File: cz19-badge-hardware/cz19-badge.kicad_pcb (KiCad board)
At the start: 4 copper layers, 169 x 56 mm, 210 parts, among them J1 USB_B_Micro, Q1 MMBT2222A, Q2 MMBT2222A, Q3 FDS8896, U1 CH340C, U2 ESP32-WROOM-32D, U3 AMS1117

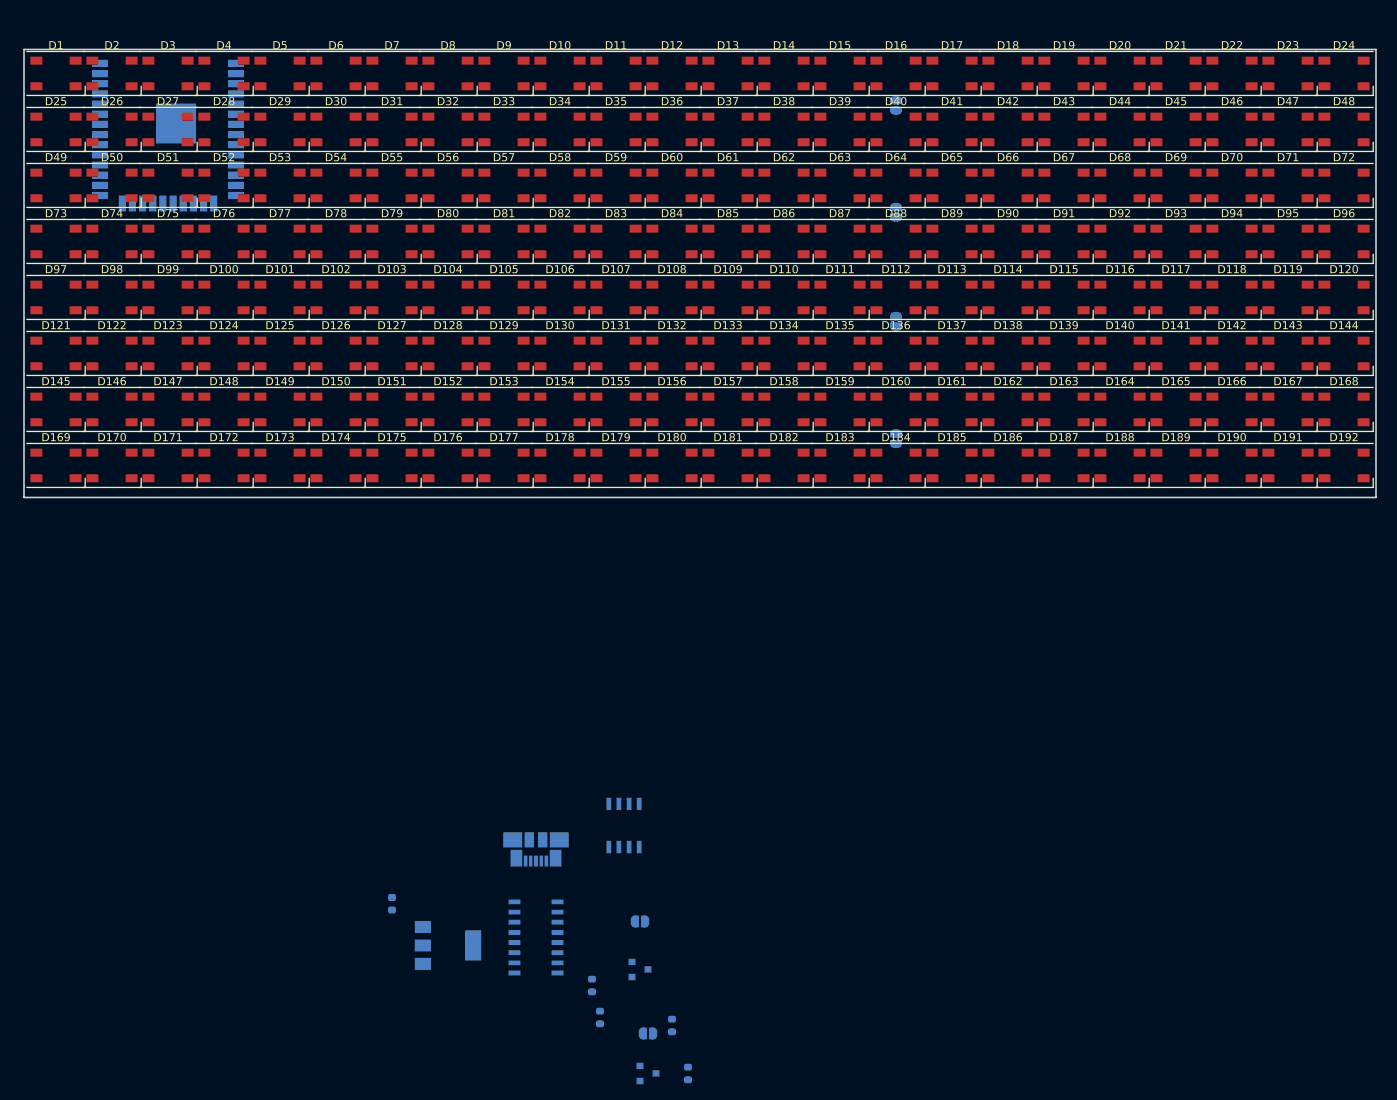
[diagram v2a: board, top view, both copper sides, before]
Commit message: Added battery, organised components, layed out PCB. Working on PCB traces of LED matrix
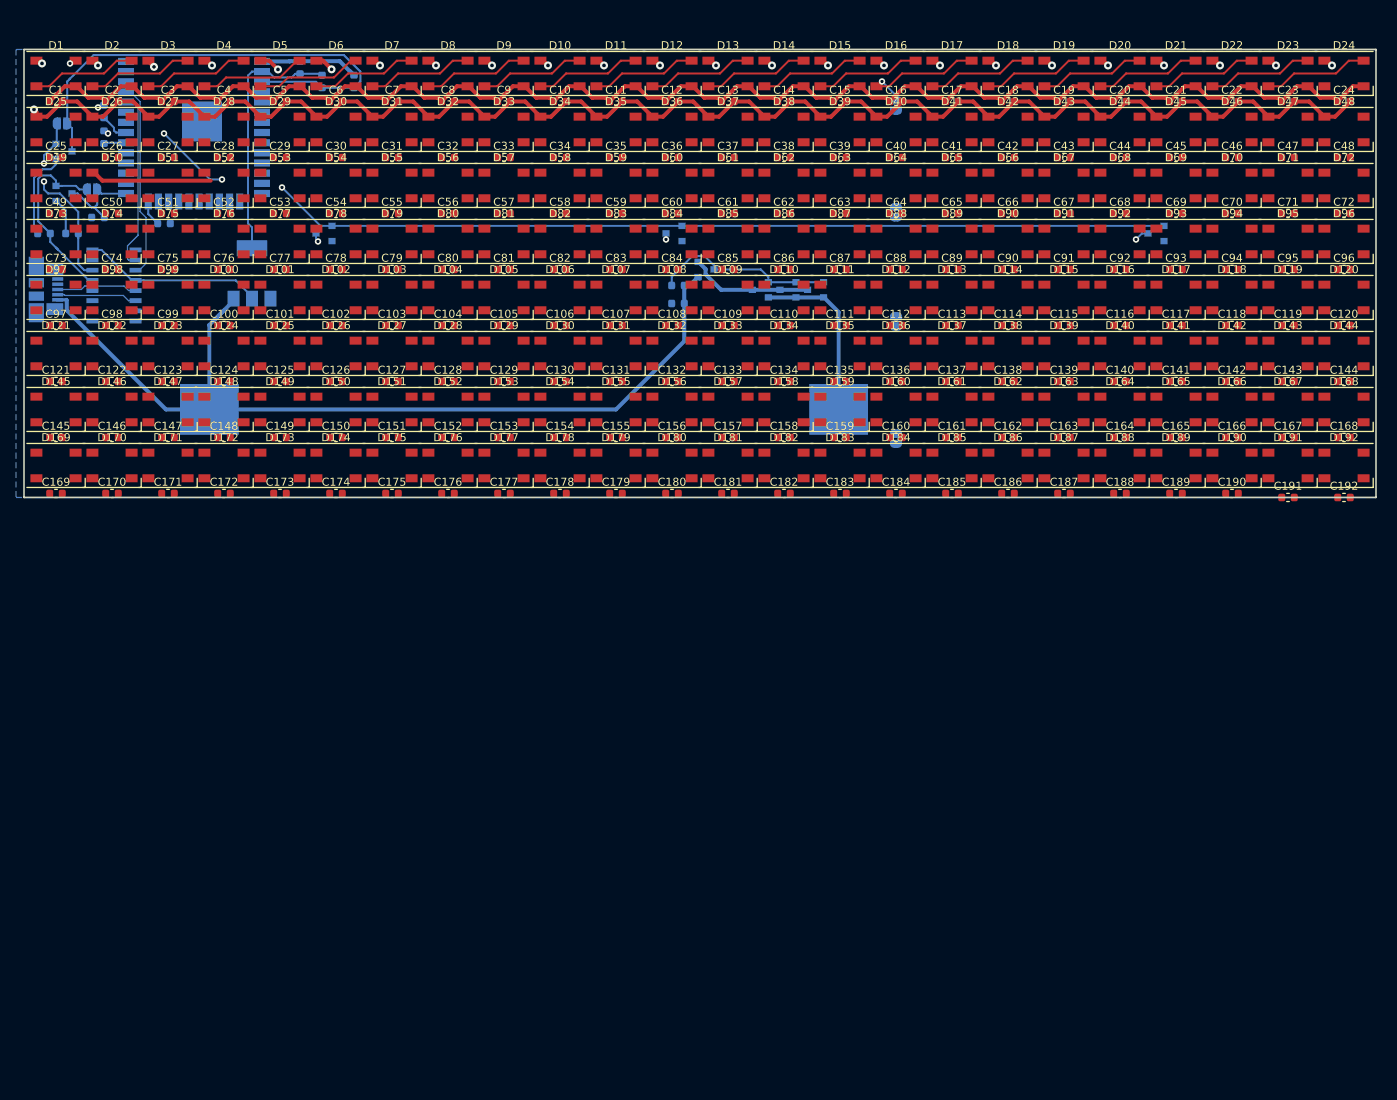
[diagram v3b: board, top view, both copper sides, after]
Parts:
- removed R2: 10k, Resistor_SMD:R_0603_1608Metric
- added BT1: Battery, LiPoHolder:BatteryHolder_Keystone_1042_1x18650, B.Cu at (82.5, 67.0)
- added C1: 100nF, Capacitor_SMD:C_0603_1608Metric, F.Cu at (24.0, 28.5)
- added C10: 100nF, Capacitor_SMD:C_0603_1608Metric, F.Cu at (87.0, 28.5)
- added C100: 100nF, Capacitor_SMD:C_0603_1608Metric, F.Cu at (45.0, 56.5)
- added C101: 100nF, Capacitor_SMD:C_0603_1608Metric, F.Cu at (52.0, 56.5)
- added C102: 100nF, Capacitor_SMD:C_0603_1608Metric, F.Cu at (59.0, 56.5)
- added C103: 100nF, Capacitor_SMD:C_0603_1608Metric, F.Cu at (66.0, 56.5)
- added C104: 100nF, Capacitor_SMD:C_0603_1608Metric, F.Cu at (73.0, 56.5)
- added C105: 100nF, Capacitor_SMD:C_0603_1608Metric, F.Cu at (80.0, 56.5)
- added C106: 100nF, Capacitor_SMD:C_0603_1608Metric, F.Cu at (87.0, 56.5)
- added C107: 100nF, Capacitor_SMD:C_0603_1608Metric, F.Cu at (94.0, 56.5)
- added C108: 100nF, Capacitor_SMD:C_0603_1608Metric, F.Cu at (101.0, 56.5)
- added C109: 100nF, Capacitor_SMD:C_0603_1608Metric, F.Cu at (108.0, 56.5)
- added C11: 100nF, Capacitor_SMD:C_0603_1608Metric, F.Cu at (94.0, 28.5)
- added C110: 100nF, Capacitor_SMD:C_0603_1608Metric, F.Cu at (115.0, 56.5)
- added C111: 100nF, Capacitor_SMD:C_0603_1608Metric, F.Cu at (122.0, 56.5)
- added C112: 100nF, Capacitor_SMD:C_0603_1608Metric, F.Cu at (129.0, 56.5)
- added C113: 100nF, Capacitor_SMD:C_0603_1608Metric, F.Cu at (136.0, 56.5)
- added C114: 100nF, Capacitor_SMD:C_0603_1608Metric, F.Cu at (143.0, 56.5)
- added C115: 100nF, Capacitor_SMD:C_0603_1608Metric, F.Cu at (150.0, 56.5)
- added C116: 100nF, Capacitor_SMD:C_0603_1608Metric, F.Cu at (157.0, 56.5)
- added C117: 100nF, Capacitor_SMD:C_0603_1608Metric, F.Cu at (164.0, 56.5)
- added C118: 100nF, Capacitor_SMD:C_0603_1608Metric, F.Cu at (171.0, 56.5)
- added C119: 100nF, Capacitor_SMD:C_0603_1608Metric, F.Cu at (178.0, 56.5)
- added C12: 100nF, Capacitor_SMD:C_0603_1608Metric, F.Cu at (101.0, 28.5)
- added C120: 100nF, Capacitor_SMD:C_0603_1608Metric, F.Cu at (185.0, 56.5)
- added C121: 100nF, Capacitor_SMD:C_0603_1608Metric, F.Cu at (24.0, 63.5)
- added C122: 100nF, Capacitor_SMD:C_0603_1608Metric, F.Cu at (31.0, 63.5)
- added C123: 100nF, Capacitor_SMD:C_0603_1608Metric, F.Cu at (38.0, 63.5)
- added C124: 100nF, Capacitor_SMD:C_0603_1608Metric, F.Cu at (45.0, 63.5)
- added C125: 100nF, Capacitor_SMD:C_0603_1608Metric, F.Cu at (52.0, 63.5)
- added C126: 100nF, Capacitor_SMD:C_0603_1608Metric, F.Cu at (59.0, 63.5)
- added C127: 100nF, Capacitor_SMD:C_0603_1608Metric, F.Cu at (66.0, 63.5)
- added C128: 100nF, Capacitor_SMD:C_0603_1608Metric, F.Cu at (73.0, 63.5)
- added C129: 100nF, Capacitor_SMD:C_0603_1608Metric, F.Cu at (80.0, 63.5)
- added C13: 100nF, Capacitor_SMD:C_0603_1608Metric, F.Cu at (108.0, 28.5)
- added C130: 100nF, Capacitor_SMD:C_0603_1608Metric, F.Cu at (87.0, 63.5)
- added C131: 100nF, Capacitor_SMD:C_0603_1608Metric, F.Cu at (94.0, 63.5)
- added C132: 100nF, Capacitor_SMD:C_0603_1608Metric, F.Cu at (101.0, 63.5)
- added C133: 100nF, Capacitor_SMD:C_0603_1608Metric, F.Cu at (108.0, 63.5)
- added C134: 100nF, Capacitor_SMD:C_0603_1608Metric, F.Cu at (115.0, 63.5)
- added C135: 100nF, Capacitor_SMD:C_0603_1608Metric, F.Cu at (122.0, 63.5)
- added C136: 100nF, Capacitor_SMD:C_0603_1608Metric, F.Cu at (129.0, 63.5)
- added C137: 100nF, Capacitor_SMD:C_0603_1608Metric, F.Cu at (136.0, 63.5)
- added C138: 100nF, Capacitor_SMD:C_0603_1608Metric, F.Cu at (143.0, 63.5)
- added C139: 100nF, Capacitor_SMD:C_0603_1608Metric, F.Cu at (150.0, 63.5)
- added C14: 100nF, Capacitor_SMD:C_0603_1608Metric, F.Cu at (115.0, 28.5)
- added C140: 100nF, Capacitor_SMD:C_0603_1608Metric, F.Cu at (157.0, 63.5)
- added C141: 100nF, Capacitor_SMD:C_0603_1608Metric, F.Cu at (164.0, 63.5)
- added C142: 100nF, Capacitor_SMD:C_0603_1608Metric, F.Cu at (171.0, 63.5)
- added C143: 100nF, Capacitor_SMD:C_0603_1608Metric, F.Cu at (178.0, 63.5)
- added C144: 100nF, Capacitor_SMD:C_0603_1608Metric, F.Cu at (185.0, 63.5)
- added C145: 100nF, Capacitor_SMD:C_0603_1608Metric, F.Cu at (24.0, 70.5)
- added C146: 100nF, Capacitor_SMD:C_0603_1608Metric, F.Cu at (31.0, 70.5)
- added C147: 100nF, Capacitor_SMD:C_0603_1608Metric, F.Cu at (38.0, 70.5)
- added C148: 100nF, Capacitor_SMD:C_0603_1608Metric, F.Cu at (45.0, 70.5)
- added C149: 100nF, Capacitor_SMD:C_0603_1608Metric, F.Cu at (52.0, 70.5)
- added C15: 100nF, Capacitor_SMD:C_0603_1608Metric, F.Cu at (122.0, 28.5)
- added C150: 100nF, Capacitor_SMD:C_0603_1608Metric, F.Cu at (59.0, 70.5)
- added C151: 100nF, Capacitor_SMD:C_0603_1608Metric, F.Cu at (66.0, 70.5)
- added C152: 100nF, Capacitor_SMD:C_0603_1608Metric, F.Cu at (73.0, 70.5)
- added C153: 100nF, Capacitor_SMD:C_0603_1608Metric, F.Cu at (80.0, 70.5)
- added C154: 100nF, Capacitor_SMD:C_0603_1608Metric, F.Cu at (87.0, 70.5)
- added C155: 100nF, Capacitor_SMD:C_0603_1608Metric, F.Cu at (94.0, 70.5)
- added C156: 100nF, Capacitor_SMD:C_0603_1608Metric, F.Cu at (101.0, 70.5)
- added C157: 100nF, Capacitor_SMD:C_0603_1608Metric, F.Cu at (108.0, 70.5)
- added C158: 100nF, Capacitor_SMD:C_0603_1608Metric, F.Cu at (115.0, 70.5)
- added C159: 100nF, Capacitor_SMD:C_0603_1608Metric, F.Cu at (122.0, 70.5)
- added C16: 100nF, Capacitor_SMD:C_0603_1608Metric, F.Cu at (129.0, 28.5)
- added C160: 100nF, Capacitor_SMD:C_0603_1608Metric, F.Cu at (129.0, 70.5)
- added C161: 100nF, Capacitor_SMD:C_0603_1608Metric, F.Cu at (136.0, 70.5)
- added C162: 100nF, Capacitor_SMD:C_0603_1608Metric, F.Cu at (143.0, 70.5)
- added C163: 100nF, Capacitor_SMD:C_0603_1608Metric, F.Cu at (150.0, 70.5)
- added C164: 100nF, Capacitor_SMD:C_0603_1608Metric, F.Cu at (157.0, 70.5)
- added C165: 100nF, Capacitor_SMD:C_0603_1608Metric, F.Cu at (164.0, 70.5)
- added C166: 100nF, Capacitor_SMD:C_0603_1608Metric, F.Cu at (171.0, 70.5)
- added C167: 100nF, Capacitor_SMD:C_0603_1608Metric, F.Cu at (178.0, 70.5)
- added C168: 100nF, Capacitor_SMD:C_0603_1608Metric, F.Cu at (185.0, 70.5)
- added C169: 100nF, Capacitor_SMD:C_0603_1608Metric, F.Cu at (24.0, 77.5)
- added C17: 100nF, Capacitor_SMD:C_0603_1608Metric, F.Cu at (136.0, 28.5)
- added C170: 100nF, Capacitor_SMD:C_0603_1608Metric, F.Cu at (31.0, 77.5)
- added C171: 100nF, Capacitor_SMD:C_0603_1608Metric, F.Cu at (38.0, 77.5)
- added C172: 100nF, Capacitor_SMD:C_0603_1608Metric, F.Cu at (45.0, 77.5)
- added C173: 100nF, Capacitor_SMD:C_0603_1608Metric, F.Cu at (52.0, 77.5)
- added C174: 100nF, Capacitor_SMD:C_0603_1608Metric, F.Cu at (59.0, 77.5)
- added C175: 100nF, Capacitor_SMD:C_0603_1608Metric, F.Cu at (66.0, 77.5)
- added C176: 100nF, Capacitor_SMD:C_0603_1608Metric, F.Cu at (73.0, 77.5)
- added C177: 100nF, Capacitor_SMD:C_0603_1608Metric, F.Cu at (80.0, 77.5)
- added C178: 100nF, Capacitor_SMD:C_0603_1608Metric, F.Cu at (87.0, 77.5)
- added C179: 100nF, Capacitor_SMD:C_0603_1608Metric, F.Cu at (94.0, 77.5)
- added C18: 100nF, Capacitor_SMD:C_0603_1608Metric, F.Cu at (143.0, 28.5)
- added C180: 100nF, Capacitor_SMD:C_0603_1608Metric, F.Cu at (101.0, 77.5)
- added C181: 100nF, Capacitor_SMD:C_0603_1608Metric, F.Cu at (108.0, 77.5)
- added C182: 100nF, Capacitor_SMD:C_0603_1608Metric, F.Cu at (115.0, 77.5)
- added C183: 100nF, Capacitor_SMD:C_0603_1608Metric, F.Cu at (122.0, 77.5)
- added C184: 100nF, Capacitor_SMD:C_0603_1608Metric, F.Cu at (129.0, 77.5)
- added C185: 100nF, Capacitor_SMD:C_0603_1608Metric, F.Cu at (136.0, 77.5)
- added C186: 100nF, Capacitor_SMD:C_0603_1608Metric, F.Cu at (143.0, 77.5)
- added C187: 100nF, Capacitor_SMD:C_0603_1608Metric, F.Cu at (150.0, 77.5)
- added C188: 100nF, Capacitor_SMD:C_0603_1608Metric, F.Cu at (157.0, 77.5)
- added C189: 100nF, Capacitor_SMD:C_0603_1608Metric, F.Cu at (164.0, 77.5)
- added C19: 100nF, Capacitor_SMD:C_0603_1608Metric, F.Cu at (150.0, 28.5)
- added C190: 100nF, Capacitor_SMD:C_0603_1608Metric, F.Cu at (171.0, 77.5)
- added C191: 100nF, Capacitor_SMD:C_0603_1608Metric, F.Cu at (178.0, 78.0)
- added C192: 100nF, Capacitor_SMD:C_0603_1608Metric, F.Cu at (185.0, 78.0)
- added C193: 100nF, Capacitor_SMD:C_0603_1608Metric, B.Cu at (61.2, 26.0)
- added C194: 100nF, Capacitor_SMD:C_0603_1608Metric, B.Cu at (54.5, 24.2)
- added C2: 100nF, Capacitor_SMD:C_0603_1608Metric, F.Cu at (31.0, 28.5)
- added C20: 100nF, Capacitor_SMD:C_0603_1608Metric, F.Cu at (157.0, 28.5)
- added C21: 100nF, Capacitor_SMD:C_0603_1608Metric, F.Cu at (164.0, 28.5)
- added C22: 100nF, Capacitor_SMD:C_0603_1608Metric, F.Cu at (171.0, 28.5)
- added C23: 100nF, Capacitor_SMD:C_0603_1608Metric, F.Cu at (178.0, 28.5)
- added C24: 100nF, Capacitor_SMD:C_0603_1608Metric, F.Cu at (185.0, 28.5)
- added C25: 100nF, Capacitor_SMD:C_0603_1608Metric, F.Cu at (24.0, 35.5)
- added C26: 100nF, Capacitor_SMD:C_0603_1608Metric, F.Cu at (31.0, 35.5)
- added C27: 100nF, Capacitor_SMD:C_0603_1608Metric, F.Cu at (38.0, 35.5)
- added C28: 100nF, Capacitor_SMD:C_0603_1608Metric, F.Cu at (45.0, 35.5)
- added C29: 100nF, Capacitor_SMD:C_0603_1608Metric, F.Cu at (52.0, 35.5)
- added C3: 100nF, Capacitor_SMD:C_0603_1608Metric, F.Cu at (38.0, 28.5)
- added C30: 100nF, Capacitor_SMD:C_0603_1608Metric, F.Cu at (59.0, 35.5)
- added C31: 100nF, Capacitor_SMD:C_0603_1608Metric, F.Cu at (66.0, 35.5)
- added C32: 100nF, Capacitor_SMD:C_0603_1608Metric, F.Cu at (73.0, 35.5)
- added C33: 100nF, Capacitor_SMD:C_0603_1608Metric, F.Cu at (80.0, 35.5)
- added C34: 100nF, Capacitor_SMD:C_0603_1608Metric, F.Cu at (87.0, 35.5)
- added C35: 100nF, Capacitor_SMD:C_0603_1608Metric, F.Cu at (94.0, 35.5)
- added C36: 100nF, Capacitor_SMD:C_0603_1608Metric, F.Cu at (101.0, 35.5)
- added C37: 100nF, Capacitor_SMD:C_0603_1608Metric, F.Cu at (108.0, 35.5)
- added C38: 100nF, Capacitor_SMD:C_0603_1608Metric, F.Cu at (115.0, 35.5)
- added C39: 100nF, Capacitor_SMD:C_0603_1608Metric, F.Cu at (122.0, 35.5)
- added C4: 100nF, Capacitor_SMD:C_0603_1608Metric, F.Cu at (45.0, 28.5)
- added C40: 100nF, Capacitor_SMD:C_0603_1608Metric, F.Cu at (129.0, 35.5)
- added C41: 100nF, Capacitor_SMD:C_0603_1608Metric, F.Cu at (136.0, 35.5)
- added C42: 100nF, Capacitor_SMD:C_0603_1608Metric, F.Cu at (143.0, 35.5)
- added C43: 100nF, Capacitor_SMD:C_0603_1608Metric, F.Cu at (150.0, 35.5)
- added C44: 100nF, Capacitor_SMD:C_0603_1608Metric, F.Cu at (157.0, 35.5)
- added C45: 100nF, Capacitor_SMD:C_0603_1608Metric, F.Cu at (164.0, 35.5)
- added C46: 100nF, Capacitor_SMD:C_0603_1608Metric, F.Cu at (171.0, 35.5)
- added C47: 100nF, Capacitor_SMD:C_0603_1608Metric, F.Cu at (178.0, 35.5)
- added C48: 100nF, Capacitor_SMD:C_0603_1608Metric, F.Cu at (185.0, 35.5)
- added C49: 100nF, Capacitor_SMD:C_0603_1608Metric, F.Cu at (24.0, 42.5)
- added C5: 100nF, Capacitor_SMD:C_0603_1608Metric, F.Cu at (52.0, 28.5)
- added C50: 100nF, Capacitor_SMD:C_0603_1608Metric, F.Cu at (31.0, 42.5)
- added C51: 100nF, Capacitor_SMD:C_0603_1608Metric, F.Cu at (38.0, 42.5)
- added C52: 100nF, Capacitor_SMD:C_0603_1608Metric, F.Cu at (45.0, 42.5)
- added C53: 100nF, Capacitor_SMD:C_0603_1608Metric, F.Cu at (52.0, 42.5)
- added C54: 100nF, Capacitor_SMD:C_0603_1608Metric, F.Cu at (59.0, 42.5)
- added C55: 100nF, Capacitor_SMD:C_0603_1608Metric, F.Cu at (66.0, 42.5)
- added C56: 100nF, Capacitor_SMD:C_0603_1608Metric, F.Cu at (73.0, 42.5)
- added C57: 100nF, Capacitor_SMD:C_0603_1608Metric, F.Cu at (80.0, 42.5)
- added C58: 100nF, Capacitor_SMD:C_0603_1608Metric, F.Cu at (87.0, 42.5)
- added C59: 100nF, Capacitor_SMD:C_0603_1608Metric, F.Cu at (94.0, 42.5)
- added C6: 100nF, Capacitor_SMD:C_0603_1608Metric, F.Cu at (59.0, 28.5)
- added C60: 100nF, Capacitor_SMD:C_0603_1608Metric, F.Cu at (101.0, 42.5)
- added C61: 100nF, Capacitor_SMD:C_0603_1608Metric, F.Cu at (108.0, 42.5)
- added C62: 100nF, Capacitor_SMD:C_0603_1608Metric, F.Cu at (115.0, 42.5)
- added C63: 100nF, Capacitor_SMD:C_0603_1608Metric, F.Cu at (122.0, 42.5)
- added C64: 100nF, Capacitor_SMD:C_0603_1608Metric, F.Cu at (129.0, 42.5)
- added C65: 100nF, Capacitor_SMD:C_0603_1608Metric, F.Cu at (136.0, 42.5)
- added C66: 100nF, Capacitor_SMD:C_0603_1608Metric, F.Cu at (143.0, 42.5)
- added C67: 100nF, Capacitor_SMD:C_0603_1608Metric, F.Cu at (150.0, 42.5)
- added C68: 100nF, Capacitor_SMD:C_0603_1608Metric, F.Cu at (157.0, 42.5)
- added C69: 100nF, Capacitor_SMD:C_0603_1608Metric, F.Cu at (164.0, 42.5)
- added C7: 100nF, Capacitor_SMD:C_0603_1608Metric, F.Cu at (66.0, 28.5)
- added C70: 100nF, Capacitor_SMD:C_0603_1608Metric, F.Cu at (171.0, 42.5)
- added C71: 100nF, Capacitor_SMD:C_0603_1608Metric, F.Cu at (178.0, 42.5)
- added C72: 100nF, Capacitor_SMD:C_0603_1608Metric, F.Cu at (185.0, 42.5)
- added C73: 100nF, Capacitor_SMD:C_0603_1608Metric, F.Cu at (24.0, 49.5)
- added C74: 100nF, Capacitor_SMD:C_0603_1608Metric, F.Cu at (31.0, 49.5)
- added C75: 100nF, Capacitor_SMD:C_0603_1608Metric, F.Cu at (38.0, 49.5)
- added C76: 100nF, Capacitor_SMD:C_0603_1608Metric, F.Cu at (45.0, 49.5)
- added C77: 100nF, Capacitor_SMD:C_0603_1608Metric, F.Cu at (52.0, 49.5)
- added C78: 100nF, Capacitor_SMD:C_0603_1608Metric, F.Cu at (59.0, 49.5)
- added C79: 100nF, Capacitor_SMD:C_0603_1608Metric, F.Cu at (66.0, 49.5)
- added C8: 100nF, Capacitor_SMD:C_0603_1608Metric, F.Cu at (73.0, 28.5)
- added C80: 100nF, Capacitor_SMD:C_0603_1608Metric, F.Cu at (73.0, 49.5)
- added C81: 100nF, Capacitor_SMD:C_0603_1608Metric, F.Cu at (80.0, 49.5)
- added C82: 100nF, Capacitor_SMD:C_0603_1608Metric, F.Cu at (87.0, 49.5)
- added C83: 100nF, Capacitor_SMD:C_0603_1608Metric, F.Cu at (94.0, 49.5)
- added C84: 100nF, Capacitor_SMD:C_0603_1608Metric, F.Cu at (101.0, 49.5)
- added C85: 100nF, Capacitor_SMD:C_0603_1608Metric, F.Cu at (108.0, 49.5)
- added C86: 100nF, Capacitor_SMD:C_0603_1608Metric, F.Cu at (115.0, 49.5)
- added C87: 100nF, Capacitor_SMD:C_0603_1608Metric, F.Cu at (122.0, 49.5)
- added C88: 100nF, Capacitor_SMD:C_0603_1608Metric, F.Cu at (129.0, 49.5)
- added C89: 100nF, Capacitor_SMD:C_0603_1608Metric, F.Cu at (136.0, 49.5)
- added C9: 100nF, Capacitor_SMD:C_0603_1608Metric, F.Cu at (80.0, 28.5)
- added C90: 100nF, Capacitor_SMD:C_0603_1608Metric, F.Cu at (143.0, 49.5)
- added C91: 100nF, Capacitor_SMD:C_0603_1608Metric, F.Cu at (150.0, 49.5)
- added C92: 100nF, Capacitor_SMD:C_0603_1608Metric, F.Cu at (157.0, 49.5)
- added C93: 100nF, Capacitor_SMD:C_0603_1608Metric, F.Cu at (164.0, 49.5)
- added C94: 100nF, Capacitor_SMD:C_0603_1608Metric, F.Cu at (171.0, 49.5)
- added C95: 100nF, Capacitor_SMD:C_0603_1608Metric, F.Cu at (178.0, 49.5)
- added C96: 100nF, Capacitor_SMD:C_0603_1608Metric, F.Cu at (185.0, 49.5)
- added C97: 100nF, Capacitor_SMD:C_0603_1608Metric, F.Cu at (24.0, 56.5)
- added C98: 100nF, Capacitor_SMD:C_0603_1608Metric, F.Cu at (31.0, 56.5)
- added C99: 100nF, Capacitor_SMD:C_0603_1608Metric, F.Cu at (38.0, 56.5)
- added Q4: AO3400 (A09T), Package_TO_SOT_SMD:SOT-23, B.Cu at (25.0, 34.8)
- added Q5: AO3400 (A09T), Package_TO_SOT_SMD:SOT-23, B.Cu at (161.5, 45.0)
- added Q6: AO3400 (A09T), Package_TO_SOT_SMD:SOT-23, B.Cu at (112.0, 52.0)
- added Q7: AO3400 (A09T), Package_TO_SOT_SMD:SOT-23, B.Cu at (115.5, 52.0)
- added Q8: AO3400 (A09T), Package_TO_SOT_SMD:SOT-23, B.Cu at (105.2, 49.5)
- added Q9: AO3400 (A09T), Package_TO_SOT_SMD:SOT-23, B.Cu at (118.9, 52.0)
- added R10: 10k, Resistor_SMD:R_0603_1608Metric, B.Cu at (101.8, 53.8)
- added R6: 10k, Resistor_SMD:R_0603_1608Metric, B.Cu at (37.5, 43.8)
- added R7: 10k, Resistor_SMD:R_0603_1608Metric, B.Cu at (101.8, 51.5)
- added R8: 10k, Resistor_SMD:R_0603_1608Metric, B.Cu at (30.0, 33.0)
- added R9: 10k, Resistor_SMD:R_0603_1608Metric, B.Cu at (30.0, 29.8)
- Q1, Q2: value MMBT2222A -> AO3400 (A09T)
- Q3: value FDS8896 -> AO3400 (A09T); footprint Package_SO:SOIC-8_3.9x4.9mm_P1.27mm -> Package_TO_SOT_SMD:SOT-23
- U2: value ESP32-WROOM-32D -> AMS1117; footprint RF_Module:ESP32-WROOM-32 -> Package_TO_SOT_SMD:SOT-223-3_TabPin2
- U3: value AMS1117 -> ESP32-WROOM-32D; footprint Package_TO_SOT_SMD:SOT-223-3_TabPin2 -> RF_Module:ESP32-WROOM-32
- moved JP6 135.3 mm to (24.8, 31.2), turned to 180 degrees
- moved Q2 132.0 mm to (25.0, 40.0)
- moved R5 130.0 mm to (29.2, 43.0), turned to 0 degrees
- moved R1 124.2 mm to (26.0, 45.0), turned to 180 degrees
- moved R3 116.3 mm to (22.5, 45.0), turned to 0 degrees
- moved JP5 114.3 mm to (28.5, 39.5), turned to 180 degrees
- moved U3 107.1 mm to (41.2, 31.8), turned to 180 degrees
- moved R4 103.2 mm to (57.2, 26.0)
- moved Q1 100.1 mm to (57.5, 45.0), turned to 180 degrees
- moved U1 97.1 mm to (31.2, 51.5), turned to 180 degrees
- moved J1 93.0 mm to (22.8, 52.0), turned to 90 degrees
- moved Q3 74.3 mm to (101.2, 45.0), turned to 180 degrees
- moved U2 20.8 mm to (48.5, 50.0), turned to 90 degrees
- turned JP1 to 270 degrees
- turned JP2 to 270 degrees
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- renumbered JP3 to JP1, JP4 to JP2, JP5 to JP3, JP6 to JP4, JP1 to JP5, JP2 to JP6
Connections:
- net Net-(J1-Pad2) renamed USB_DN
- net Net-(J1-Pad3) renamed USB_DP
- D1 pad 3: GND -> LED_GND
- D10 pad 3: GND -> LED_GND
- D100 pad 3: GND -> LED_GND
- D101 pad 3: GND -> LED_GND
- D102 pad 3: GND -> LED_GND
- D103 pad 3: GND -> LED_GND
- D104 pad 3: GND -> LED_GND
- D105 pad 3: GND -> LED_GND
- D106 pad 3: GND -> LED_GND
- D107 pad 3: GND -> LED_GND
- D108 pad 3: GND -> LED_GND
- D109 pad 3: GND -> LED_GND
- D11 pad 3: GND -> LED_GND
- D110 pad 3: GND -> LED_GND
- D111 pad 3: GND -> LED_GND
- D112 pad 3: GND -> LED_GND
- D113 pad 3: GND -> LED_GND
- D114 pad 3: GND -> LED_GND
- D115 pad 3: GND -> LED_GND
- D116 pad 3: GND -> LED_GND
- D117 pad 3: GND -> LED_GND
- D118 pad 3: GND -> LED_GND
- D119 pad 3: GND -> LED_GND
- D12 pad 3: GND -> LED_GND
- D120 pad 3: GND -> LED_GND
- D121 pad 3: GND -> LED_GND
- D122 pad 3: GND -> LED_GND
- D123 pad 3: GND -> LED_GND
- D124 pad 3: GND -> LED_GND
- D125 pad 3: GND -> LED_GND
- D126 pad 3: GND -> LED_GND
- D127 pad 3: GND -> LED_GND
- D128 pad 3: GND -> LED_GND
- D129 pad 3: GND -> LED_GND
- D13 pad 3: GND -> LED_GND
- D130 pad 3: GND -> LED_GND
- D131 pad 3: GND -> LED_GND
- D132 pad 3: GND -> LED_GND
- D133 pad 3: GND -> LED_GND
- D134 pad 3: GND -> LED_GND
- D135 pad 3: GND -> LED_GND
- D136 pad 3: GND -> LED_GND
- D137 pad 3: GND -> LED_GND
- D138 pad 3: GND -> LED_GND
- D139 pad 3: GND -> LED_GND
- D14 pad 3: GND -> LED_GND
- D140 pad 3: GND -> LED_GND
- D141 pad 3: GND -> LED_GND
- D142 pad 3: GND -> LED_GND
- D143 pad 3: GND -> LED_GND
- D144 pad 3: GND -> LED_GND
- D145 pad 3: GND -> LED_GND
- D146 pad 3: GND -> LED_GND
- D147 pad 3: GND -> LED_GND
- D148 pad 3: GND -> LED_GND
- D149 pad 3: GND -> LED_GND
- D15 pad 3: GND -> LED_GND
- D150 pad 3: GND -> LED_GND
- D151 pad 3: GND -> LED_GND
- D152 pad 3: GND -> LED_GND
- D153 pad 3: GND -> LED_GND
- D154 pad 3: GND -> LED_GND
- D155 pad 3: GND -> LED_GND
- D156 pad 3: GND -> LED_GND
- D157 pad 3: GND -> LED_GND
- D158 pad 3: GND -> LED_GND
- D159 pad 3: GND -> LED_GND
- D16 pad 3: GND -> LED_GND
- D160 pad 3: GND -> LED_GND
- D161 pad 3: GND -> LED_GND
- D162 pad 3: GND -> LED_GND
- D163 pad 3: GND -> LED_GND
- D164 pad 3: GND -> LED_GND
- D165 pad 3: GND -> LED_GND
- D166 pad 3: GND -> LED_GND
- D167 pad 3: GND -> LED_GND
- D168 pad 3: GND -> LED_GND
- D169 pad 3: GND -> LED_GND
- D169 pad 4: LEDS_OUT -> (no net)
- D17 pad 3: GND -> LED_GND
- D170 pad 3: GND -> LED_GND
- D171 pad 3: GND -> LED_GND
- D172 pad 3: GND -> LED_GND
- D173 pad 3: GND -> LED_GND
- D174 pad 3: GND -> LED_GND
- D175 pad 3: GND -> LED_GND
- D176 pad 3: GND -> LED_GND
- D177 pad 3: GND -> LED_GND
- D178 pad 3: GND -> LED_GND
- D179 pad 3: GND -> LED_GND
- D18 pad 3: GND -> LED_GND
- D180 pad 3: GND -> LED_GND
- D181 pad 3: GND -> LED_GND
- D182 pad 3: GND -> LED_GND
- D183 pad 3: GND -> LED_GND
- D184 pad 3: GND -> LED_GND
- D185 pad 3: GND -> LED_GND
- D186 pad 3: GND -> LED_GND
- D187 pad 3: GND -> LED_GND
- D188 pad 3: GND -> LED_GND
- D189 pad 3: GND -> LED_GND
- D19 pad 3: GND -> LED_GND
- D190 pad 3: GND -> LED_GND
- D191 pad 3: GND -> LED_GND
- D192 pad 3: GND -> LED_GND
- D2 pad 3: GND -> LED_GND
- D20 pad 3: GND -> LED_GND
- D21 pad 3: GND -> LED_GND
- D22 pad 3: GND -> LED_GND
- D23 pad 3: GND -> LED_GND
- D24 pad 3: GND -> LED_GND
- D25 pad 3: GND -> LED_GND
- D26 pad 3: GND -> LED_GND
- D27 pad 3: GND -> LED_GND
- D28 pad 3: GND -> LED_GND
- D29 pad 3: GND -> LED_GND
- D3 pad 3: GND -> LED_GND
- D30 pad 3: GND -> LED_GND
- D31 pad 3: GND -> LED_GND
- D32 pad 3: GND -> LED_GND
- D33 pad 3: GND -> LED_GND
- D34 pad 3: GND -> LED_GND
- D35 pad 3: GND -> LED_GND
- D36 pad 3: GND -> LED_GND
- D37 pad 3: GND -> LED_GND
- D38 pad 3: GND -> LED_GND
- D39 pad 3: GND -> LED_GND
- D4 pad 3: GND -> LED_GND
- D40 pad 3: GND -> LED_GND
- D41 pad 3: GND -> LED_GND
- D42 pad 3: GND -> LED_GND
- D43 pad 3: GND -> LED_GND
- D44 pad 3: GND -> LED_GND
- D45 pad 3: GND -> LED_GND
- D46 pad 3: GND -> LED_GND
- D47 pad 3: GND -> LED_GND
- D48 pad 3: GND -> LED_GND
- D49 pad 3: GND -> LED_GND
- D5 pad 3: GND -> LED_GND
- D50 pad 3: GND -> LED_GND
- D51 pad 3: GND -> LED_GND
- D52 pad 3: GND -> LED_GND
- D53 pad 3: GND -> LED_GND
- D54 pad 3: GND -> LED_GND
- D55 pad 3: GND -> LED_GND
- D56 pad 3: GND -> LED_GND
- D57 pad 3: GND -> LED_GND
- D58 pad 3: GND -> LED_GND
- D59 pad 3: GND -> LED_GND
- D6 pad 3: GND -> LED_GND
- D60 pad 3: GND -> LED_GND
- D61 pad 3: GND -> LED_GND
- D62 pad 3: GND -> LED_GND
- D63 pad 3: GND -> LED_GND
- D64 pad 3: GND -> LED_GND
- D65 pad 3: GND -> LED_GND
- D66 pad 3: GND -> LED_GND
- D67 pad 3: GND -> LED_GND
- D68 pad 3: GND -> LED_GND
- D69 pad 3: GND -> LED_GND
- D7 pad 3: GND -> LED_GND
- D70 pad 3: GND -> LED_GND
- D71 pad 3: GND -> LED_GND
- D72 pad 3: GND -> LED_GND
- D73 pad 3: GND -> LED_GND
- D74 pad 3: GND -> LED_GND
- D75 pad 3: GND -> LED_GND
- D76 pad 3: GND -> LED_GND
- D77 pad 3: GND -> LED_GND
- D78 pad 3: GND -> LED_GND
- D79 pad 3: GND -> LED_GND
- D8 pad 3: GND -> LED_GND
- D80 pad 3: GND -> LED_GND
- D81 pad 3: GND -> LED_GND
- D82 pad 3: GND -> LED_GND
- D83 pad 3: GND -> LED_GND
- D84 pad 3: GND -> LED_GND
- D85 pad 3: GND -> LED_GND
- D86 pad 3: GND -> LED_GND
- D87 pad 3: GND -> LED_GND
- D88 pad 3: GND -> LED_GND
- D89 pad 3: GND -> LED_GND
- D9 pad 3: GND -> LED_GND
- D90 pad 3: GND -> LED_GND
- D91 pad 3: GND -> LED_GND
- D92 pad 3: GND -> LED_GND
- D93 pad 3: GND -> LED_GND
- D94 pad 3: GND -> LED_GND
- D95 pad 3: GND -> LED_GND
- D96 pad 3: GND -> LED_GND
- D97 pad 3: GND -> LED_GND
- D98 pad 3: GND -> LED_GND
- D99 pad 3: GND -> LED_GND
- J1 pad 4: Net-(J1-Pad4) -> (no net)
- JP5 pad 2: Net-(JP1-Pad2) -> Net-(JP5-Pad2)
- JP6 pad 2: Net-(JP2-Pad2) -> Net-(JP6-Pad2)
- Q1 pad 1: Net-(Q1-Pad1) -> LEDS_ENABLE
- Q1 pad 2: ESP_FLASH -> GND
- Q1 pad 3: Net-(JP1-Pad2) -> LED_GND
- Q2 pad 2: ESP_EN -> Net-(JP5-Pad2)
- Q2 pad 3: Net-(JP2-Pad2) -> ESP_FLASH
- Q3 pad 1: GND -> LEDS_ENABLE
- Q3 pad 3: GND -> LED_GND
- R1 pad 1: Net-(JP2-Pad2) -> Net-(JP6-Pad2)
- R1 pad 2: Net-(Q1-Pad1) -> Net-(Q2-Pad1)
- R3 pad 1: 3V3 -> Net-(Q4-Pad1)
- R3 pad 2: ESP_FLASH -> Net-(JP5-Pad2)
- R4 pad 1: GND -> ESP_EN
- R4 pad 2: Net-(R4-Pad2) -> 3V3
- R5 pad 1: Net-(Q2-Pad1) -> 3V3
- R5 pad 2: Net-(JP1-Pad2) -> ESP_FLASH
- U1 pad 1: Net-(U1-Pad1) -> (no net)
- U1 pad 10: Net-(U1-Pad10) -> (no net)
- U1 pad 11: Net-(U1-Pad11) -> (no net)
- U1 pad 12: Net-(U1-Pad12) -> (no net)
- U1 pad 13: Net-(JP1-Pad2) -> Net-(JP5-Pad2)
- U1 pad 14: Net-(JP2-Pad2) -> Net-(JP6-Pad2)
- U1 pad 15: Net-(U1-Pad15) -> (no net)
- U1 pad 7: Net-(U1-Pad7) -> (no net)
- U1 pad 8: Net-(U1-Pad8) -> (no net)
- U1 pad 9: Net-(U1-Pad9) -> (no net)
- U2 pad 3: ESP_EN -> 5V_USB
- U3 pad 3: 5V_USB -> ESP_EN
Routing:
- net 5V_USB: track 0.00 -> 312.3 mm
- net LED_GND: track 0.00 -> 251.8 mm, vias 0 -> 28
- net LEDS_ENABLE: track 0.00 -> 137.4 mm, vias 0 -> 4
- net ESP_EN: track 0.00 -> 62.2 mm
- net 3V3: track 0.00 -> 55.6 mm
- net GND: track 0.00 -> 27.8 mm
- net ESP_TX: track 0.00 -> 24.4 mm
- net Net-(JP5-Pad2): track 0.00 -> 23.5 mm
- net Net-(Q6-Pad1): track 0.00 -> 23.2 mm
- net Net-(JP6-Pad2): track 0.00 -> 23.0 mm, vias 0 -> 2
- net ESP_RX: track 0.00 -> 22.5 mm
- net -BATT: track 0.00 -> 21.7 mm
- net Net-(D16-Pad4): track 0.00 -> 17.2 mm, vias 0 -> 1
- net Net-(D8-Pad4): track 0.00 -> 13.2 mm
- net Net-(D7-Pad4): track 0.00 -> 13.2 mm
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- added copper zone on VCC.Cu, net 5V_USB
- added copper zone on B.Cu, net GND
- added copper zone on LGND.Cu, net LED_GND
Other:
- net class Power added: clearance 0.2, trace_width 0.5, via_dia 1, via_drill 0.45
- net class UART added: clearance 0.127, trace_width 0.127, via_dia 0.8, via_drill 0.4
- net class USB +5V added: clearance 0.2, trace_width 0.4, via_dia 0.8, via_drill 0.4
- net class USB data added: clearance 0.127, trace_width 0.127, via_dia 0.8, via_drill 0.4
- rule trace_min: 0.2 -> 0.127
- rule via_min_drill: 0.3 -> 0.2
- rule via_min_size: 0.4 -> 0.3

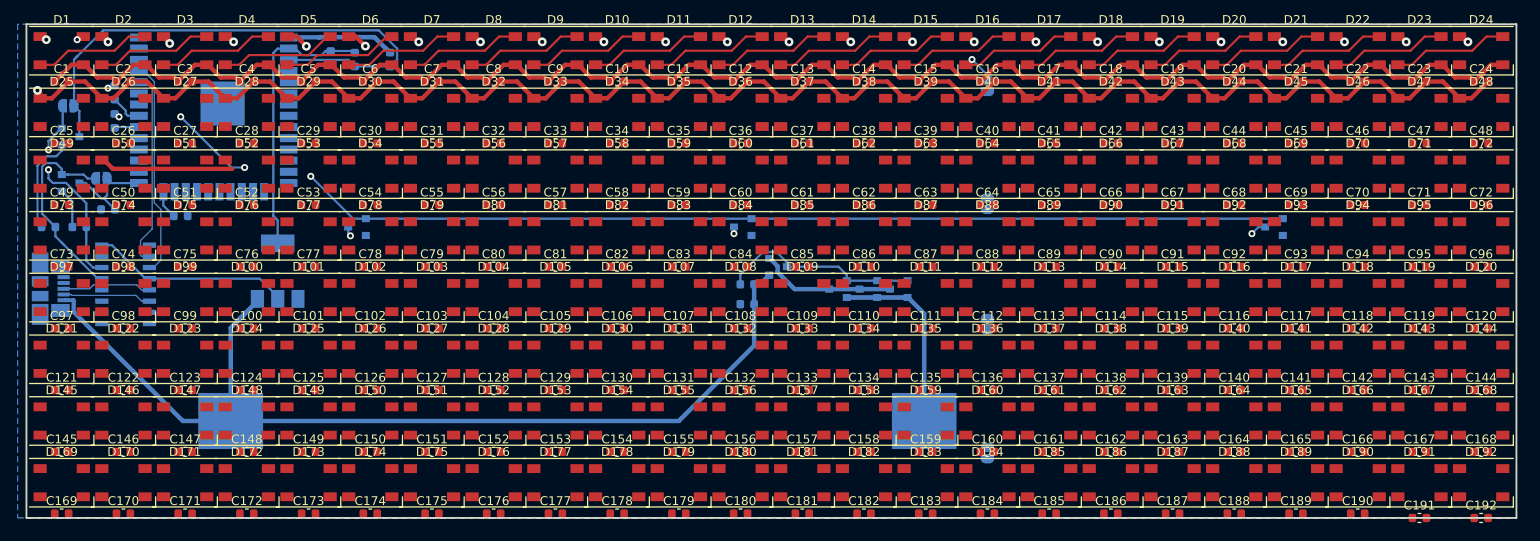
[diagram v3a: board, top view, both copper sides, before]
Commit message: Added majority of LED traces
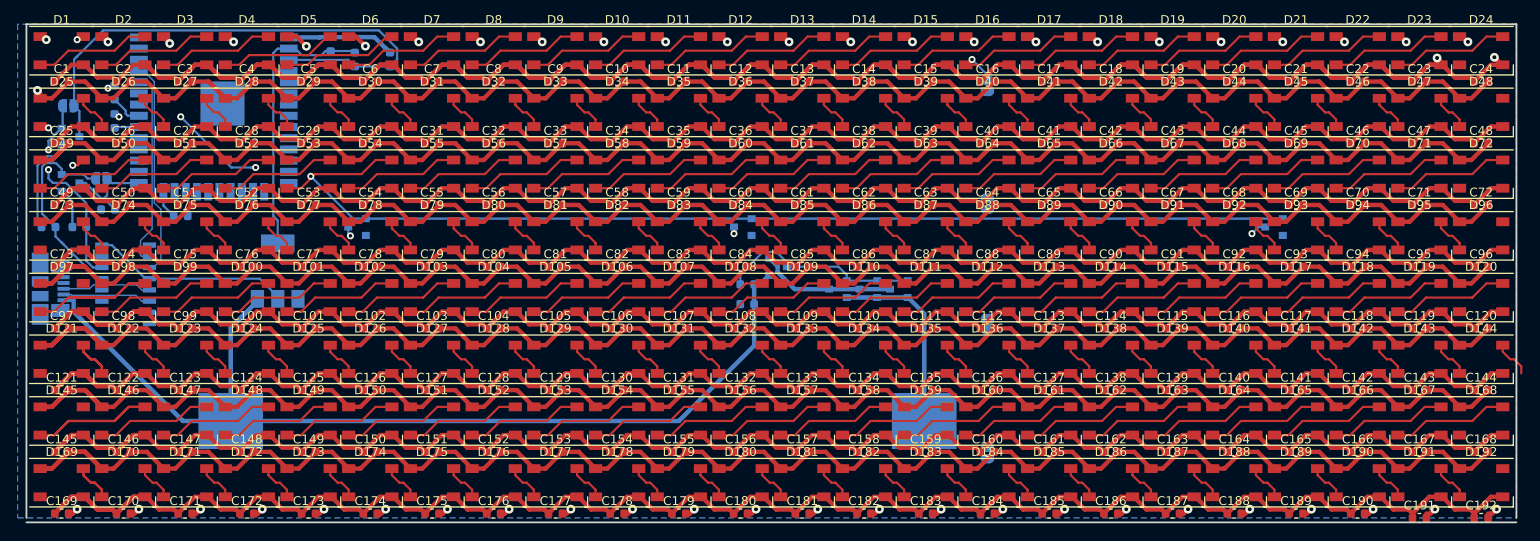
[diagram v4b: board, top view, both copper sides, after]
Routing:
- net 5V_USB: track 312.3 -> 1963.4 mm, vias 0 -> 2
- net LED_GND: track 251.8 -> 1510.5 mm, vias 28 -> 52
- net Net-(D97-Pad4): track 0.00 -> 26.5 mm
- net Net-(D145-Pad4): track 0.00 -> 26.5 mm
- net Net-(D62-Pad4): track 0.00 -> 13.2 mm
- net Net-(D61-Pad4): track 0.00 -> 13.2 mm
- net Net-(D60-Pad4): track 0.00 -> 13.2 mm
- net Net-(D59-Pad4): track 0.00 -> 13.2 mm
- net Net-(D58-Pad4): track 0.00 -> 13.2 mm
- net Net-(D57-Pad4): track 0.00 -> 13.2 mm
- net Net-(D56-Pad4): track 0.00 -> 13.2 mm
- net Net-(D55-Pad4): track 0.00 -> 13.2 mm
- net Net-(D110-Pad4): track 0.00 -> 13.2 mm
- net Net-(D109-Pad4): track 0.00 -> 13.2 mm
- net Net-(D108-Pad4): track 0.00 -> 13.2 mm
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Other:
- board size 169 x 56 mm -> 169 x 56.5 mm

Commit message: Finalised all crucial traces
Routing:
- net Net-(D73-Pad4): track 0.00 -> 8.31 mm, vias 0 -> 2
- net 5V_USB: track 1963.4 -> 1971.3 mm, vias 2 -> 9
- net LED_GND: track 1510.5 -> 1518.4 mm, vias 52 -> 59
- net Net-(D121-Pad4): track 0.00 -> 7.06 mm, vias 0 -> 2
- net Net-(D168-Pad4): track 0.00 -> 6.77 mm, vias 0 -> 2
- net Net-(D72-Pad4): track 0.00 -> 6.77 mm, vias 0 -> 2
- net Net-(D24-Pad4): track 0.00 -> 6.77 mm, vias 0 -> 2
- net -BATT: track 21.7 -> 26.6 mm
- net 3V3: track 55.6 -> 59.7 mm
- net GND: track 27.8 -> 31.5 mm
- net Net-(D136-Pad2): track 4.33 -> 7.57 mm, vias 0 -> 1
- net Net-(D88-Pad2): track 4.33 -> 7.36 mm, vias 0 -> 1
- net Net-(D184-Pad2): track 4.33 -> 7.24 mm, vias 0 -> 1
- net Net-(D40-Pad2): track 4.33 -> 7.09 mm, vias 0 -> 1
- net Net-(D120-Pad4): track 4.33 -> 6.77 mm, vias 0 -> 2
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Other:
- outline, holes or cut-outs redrawn
